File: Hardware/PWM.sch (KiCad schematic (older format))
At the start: 2 parts, among them U1 NLAS4599

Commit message: Renamed project
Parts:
- added D?: LED, symbol LED
- added R?: 250, symbol R
- added R?: 10K, symbol R
- added R?: 0, symbol R
- added TP?: TEST, symbol TEST
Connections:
- wire segments 13 -> 20
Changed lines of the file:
@@
 $Descr A4 11693 8268
 encoding utf-8
-Sheet 3 14
-Title ""
-Date ""
+Sheet 14 14
+Title "PWM Switching Circuit"
+Date "2017-05-13"
 Rev ""
-Comp ""
-Comment1 ""
+Comp "WARG"
+Comment1 "Author:Stephen Cholvat"
 Comment2 ""
 Comment3 ""
@@
 AR Path="/5919E173/5917D576" Ref="P?"  Part="1"
 AR Path="/591E6415/591EA448/5917D576" Ref="P?"  Part="1"
+AR Path="/591E6415/591EA45A/5917D576" Ref="P?"  Part="1"
+AR Path="/591E6415/591EA50E/5917D576" Ref="P?"  Part="1"
 F 0 "P?" H 6350 2600 50  0001 C CNN
 F 1 "PWM" V 6450 2400 50  0000 C CNN
@@
 AR Path="/5919E173/5917D57C" Ref="U1"  Part="1"
 AR Path="/591E6415/591EA448/5917D57C" Ref="U1"  Part="1"
+AR Path="/591E6415/591EA45A/5917D57C" Ref="U1"  Part="1"
+AR Path="/591E6415/591EA50E/5917D57C" Ref="U1"  Part="1"
 F 0 "U1" H 4500 3250 60  0000 C CNN
 F 1 "NLAS4599" H 4550 2500 60  0000 C CNN
@@
 $EndComp
 Wire Wire Line
-	4900 2500 5100 2500
-Wire Wire Line
-	5100 2500 6150 2500
+	4900 2500 6150 2500
 $Comp
 L GND #PWR?
@@
 AR Path="/5919E173/5917D836" Ref="#PWR?"  Part="1"
 AR Path="/591E6415/591EA448/5917D836" Ref="#PWR?"  Part="1"
+AR Path="/591E6415/591EA45A/5917D836" Ref="#PWR?"  Part="1"
+AR Path="/591E6415/591EA50E/5917D836" Ref="#PWR?"  Part="1"
 F 0 "#PWR?" H 5100 2450 50  0001 C CNN
 F 1 "GND" H 5100 2550 50  0000 C CNN
@@
 AR Path="/5919E173/5917D84C" Ref="#PWR?"  Part="1"
 AR Path="/591E6415/591EA448/5917D84C" Ref="#PWR?"  Part="1"
+AR Path="/591E6415/591EA45A/5917D84C" Ref="#PWR?"  Part="1"
+AR Path="/591E6415/591EA50E/5917D84C" Ref="#PWR?"  Part="1"
 F 0 "#PWR?" H 5100 1750 50  0001 C CNN
 F 1 "+5V" H 5100 2040 50  0000 C CNN
@@
 Text HLabel 5750 1950 1    60   Input ~ 0
 PWM_5V
-Text HLabel 3050 2450 0    60   Input ~ 0
+Text HLabel 2750 2450 0    60   Input ~ 0
 SEL
-Text HLabel 3050 2250 0    60   Input ~ 0
+Text HLabel 2750 2250 0    60   Input ~ 0
 PWM
-Text HLabel 3050 2150 0    60   Input ~ 0
+Text HLabel 2750 2150 0    60   Input ~ 0
 OC
 Wire Wire Line
-	3050 2150 4100 2150
-Wire Wire Line
-	3050 2250 4100 2250
-Wire Wire Line
-	3050 2450 4100 2450
+	2750 2150 4100 2150
+Wire Wire Line
+	2750 2250 4100 2250
+Wire Wire Line
+	2750 2450 3650 2450
 Wire Wire Line
 	4900 2200 4900 2300
 Wire Wire Line
 	4900 2300 6150 2300
+$Comp
+L LED D?
+U 1 1 591EF19A
+P 3550 3000
+AR Path="/591E6415/591EA448/591EF19A" Ref="D?"  Part="1"
+AR Path="/591E6415/591EA50E/591EF19A" Ref="D?"  Part="1"
+F 0 "D?" H 3550 3100 50  0000 C CNN
+F 1 "LED" H 3550 2900 50  0000 C CNN
+F 2 "" H 3550 3000 50  0000 C CNN
+F 3 "" H 3550 3000 50  0000 C CNN
+	1    3550 3000
+	0    -1   -1   0
+$EndComp
+$Comp
+L R R?
+U 1 1 591EF2D3
+P 3550 2650
+AR Path="/591E6415/591EA448/591EF2D3" Ref="R?"  Part="1"
+AR Path="/591E6415/591EA50E/591EF2D3" Ref="R?"  Part="1"
+F 0 "R?" V 3630 2650 50  0000 C CNN
+F 1 "250" V 3550 2650 50  0000 C CNN
+F 2 "" V 3480 2650 50  0000 C CNN
+F 3 "" H 3550 2650 50  0000 C CNN
+	1    3550 2650
+	1    0    0    -1
+$EndComp
+Wire Wire Line
+	3550 2800 3550 2850
+Wire Wire Line
+	3550 2450 3550 2500
+Connection ~ 3550 2450
+$Comp
+L GND #PWR?
+U 1 1 591EF3D9
+P 3350 3200
+AR Path="/591E6415/591EA448/591EF3D9" Ref="#PWR?"  Part="1"
+AR Path="/591E6415/591EA50E/591EF3D9" Ref="#PWR?"  Part="1"
+F 0 "#PWR?" H 3350 2950 50  0001 C CNN
+F 1 "GND" H 3350 3050 50  0000 C CNN
+F 2 "" H 3350 3200 50  0000 C CNN
+F 3 "" H 3350 3200 50  0000 C CNN
+	1    3350 3200
+	1    0    0    -1
+$EndComp
+Wire Wire Line
+	3550 3200 3550 3150
+$Comp
+L R R?
+U 1 1 591F0A89
+P 3150 2650
+F 0 "R?" V 3230 2650 50  0000 C CNN
+F 1 "10K" V 3150 2650 50  0000 C CNN
+F 2 "" V 3080 2650 50  0000 C CNN
+F 3 "" H 3150 2650 50  0000 C CNN
+	1    3150 2650
+	1    0    0    -1
+$EndComp
+Wire Wire Line
+	3150 3200 3550 3200
+Wire Wire Line
+	3150 2800 3150 3200
+Connection ~ 3350 3200
+Wire Wire Line
+	3150 2500 3150 2450
+Connection ~ 3150 2450
+$Comp
+L R R?
+U 1 1 591F0BAE
+P 3800 2450
+F 0 "R?" V 3880 2450 50  0000 C CNN
+F 1 "0" V 3800 2450 50  0000 C CNN
+F 2 "" V 3730 2450 50  0000 C CNN
+F 3 "" H 3800 2450 50  0000 C CNN
+	1    3800 2450
+	0    1    1    0
+$EndComp
+Wire Wire Line
+	3950 2450 4100 2450
+Connection ~ 4000 2450
+$Comp
+L TEST TP?
+U 1 1 591F0CEF
+P 4000 2600
+F 0 "TP?" H 4000 2900 50  0000 C BNN
+F 1 "TEST" H 4000 2850 50  0000 C CNN
+F 2 "" H 4000 2600 50  0000 C CNN
+F 3 "" H 4000 2600 50  0000 C CNN
+	1    4000 2600
+	-1   0    0    1
+$EndComp
+Wire Wire Line
+	4000 2600 4000 2450
 $EndSCHEMATC

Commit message: ALL THE POWER
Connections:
- net labels added: SW_5V
- net labels removed: +5V
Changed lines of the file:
@@
 LIBS:valves
 LIBS:WARG
+LIBS:ZeroPilot-cache
 EELAYER 25 0
 EELAYER END
 $Descr A4 11693 8268
 encoding utf-8
-Sheet 14 14
+Sheet 14 15
 Title "PWM Switching Circuit"
 Date "2017-05-13"
@@
 AR Path="/591E6415/591EA45A/5917D576" Ref="P?"  Part="1"
 AR Path="/591E6415/591EA50E/5917D576" Ref="P?"  Part="1"
+AR Path="/591E6415/591EA490/5917D576" Ref="P?"  Part="1"
+AR Path="/591E6415/591EA46C/5917D576" Ref="P?"  Part="1"
+AR Path="/591E6415/591EA47E/5917D576" Ref="P?"  Part="1"
+AR Path="/591E6415/591EA4A2/5917D576" Ref="P?"  Part="1"
+AR Path="/591E6415/591EA4B4/5917D576" Ref="P?"  Part="1"
+AR Path="/591E6415/591EA4C6/5917D576" Ref="P?"  Part="1"
+AR Path="/591E6415/591EA4D8/5917D576" Ref="P?"  Part="1"
+AR Path="/591E6415/591EA4EA/5917D576" Ref="P?"  Part="1"
+AR Path="/591E6415/591EA4FC/5917D576" Ref="P?"  Part="1"
 F 0 "P?" H 6350 2600 50  0001 C CNN
 F 1 "PWM" V 6450 2400 50  0000 C CNN
@@
 AR Path="/591E6415/591EA45A/5917D57C" Ref="U1"  Part="1"
 AR Path="/591E6415/591EA50E/5917D57C" Ref="U1"  Part="1"
+AR Path="/591E6415/591EA490/5917D57C" Ref="U1"  Part="1"
+AR Path="/591E6415/591EA46C/5917D57C" Ref="U1"  Part="1"
+AR Path="/591E6415/591EA47E/5917D57C" Ref="U1"  Part="1"
+AR Path="/591E6415/591EA4A2/5917D57C" Ref="U1"  Part="1"
+AR Path="/591E6415/591EA4B4/5917D57C" Ref="U1"  Part="1"
+AR Path="/591E6415/591EA4C6/5917D57C" Ref="U1"  Part="1"
+AR Path="/591E6415/591EA4D8/5917D57C" Ref="U1"  Part="1"
+AR Path="/591E6415/591EA4EA/5917D57C" Ref="U1"  Part="1"
+AR Path="/591E6415/591EA4FC/5917D57C" Ref="U1"  Part="1"
 F 0 "U1" H 4500 3250 60  0000 C CNN
 F 1 "NLAS4599" H 4550 2500 60  0000 C CNN
@@
 AR Path="/591836F4/5917D836" Ref="#PWR?"  Part="1"
 AR Path="/5919E173/5917D836" Ref="#PWR?"  Part="1"
-AR Path="/591E6415/591EA448/5917D836" Ref="#PWR?"  Part="1"
-AR Path="/591E6415/591EA45A/5917D836" Ref="#PWR?"  Part="1"
-AR Path="/591E6415/591EA50E/5917D836" Ref="#PWR?"  Part="1"
-F 0 "#PWR?" H 5100 2450 50  0001 C CNN
+AR Path="/591E6415/591EA448/5917D836" Ref="#PWR01"  Part="1"
+AR Path="/591E6415/591EA45A/5917D836" Ref="#PWR03"  Part="1"
+AR Path="/591E6415/591EA50E/5917D836" Ref="#PWR023"  Part="1"
+AR Path="/591E6415/591EA490/5917D836" Ref="#PWR09"  Part="1"
+AR Path="/591E6415/591EA46C/5917D836" Ref="#PWR05"  Part="1"
+AR Path="/591E6415/591EA47E/5917D836" Ref="#PWR07"  Part="1"
+AR Path="/591E6415/591EA4A2/5917D836" Ref="#PWR011"  Part="1"
+AR Path="/591E6415/591EA4B4/5917D836" Ref="#PWR013"  Part="1"
+AR Path="/591E6415/591EA4C6/5917D836" Ref="#PWR015"  Part="1"
+AR Path="/591E6415/591EA4D8/5917D836" Ref="#PWR017"  Part="1"
+AR Path="/591E6415/591EA4EA/5917D836" Ref="#PWR019"  Part="1"
+AR Path="/591E6415/591EA4FC/5917D836" Ref="#PWR021"  Part="1"
+F 0 "#PWR023" H 5100 2450 50  0001 C CNN
 F 1 "GND" H 5100 2550 50  0000 C CNN
 F 2 "" H 5100 2700 50  0000 C CNN
@@
 	1    0    0    -1
 $EndComp
-$Comp
-L +5V #PWR?
-U 1 1 5917D84C
-P 5100 1900
-AR Path="/5917CEAC/5917D84C" Ref="#PWR?"  Part="1"
-AR Path="/5917EAD8/5917D84C" Ref="#PWR?"  Part="1"
-AR Path="/5917F7DD/5917D84C" Ref="#PWR?"  Part="1"
-AR Path="/591836F4/5917D84C" Ref="#PWR?"  Part="1"
-AR Path="/5919E173/5917D84C" Ref="#PWR?"  Part="1"
-AR Path="/591E6415/591EA448/5917D84C" Ref="#PWR?"  Part="1"
-AR Path="/591E6415/591EA45A/5917D84C" Ref="#PWR?"  Part="1"
-AR Path="/591E6415/591EA50E/5917D84C" Ref="#PWR?"  Part="1"
-F 0 "#PWR?" H 5100 1750 50  0001 C CNN
-F 1 "+5V" H 5100 2040 50  0000 C CNN
-F 2 "" H 5100 1900 50  0000 C CNN
-F 3 "" H 5100 1900 50  0000 C CNN
-	1    5100 1900
-	1    0    0    -1
-$EndComp
 Wire Wire Line
 	4900 2200 4900 2200
@@
 Wire Wire Line
 	4900 2400 5100 2400
-Wire Wire Line
-	5100 2400 5100 1900
 Wire Wire Line
 	5100 2700 5100 2500
@@
 AR Path="/591E6415/591EA448/591EF19A" Ref="D?"  Part="1"
 AR Path="/591E6415/591EA50E/591EF19A" Ref="D?"  Part="1"
+AR Path="/591E6415/591EA490/591EF19A" Ref="D?"  Part="1"
+AR Path="/591E6415/591EA45A/591EF19A" Ref="D?"  Part="1"
+AR Path="/591E6415/591EA46C/591EF19A" Ref="D?"  Part="1"
+AR Path="/591E6415/591EA47E/591EF19A" Ref="D?"  Part="1"
+AR Path="/591E6415/591EA4A2/591EF19A" Ref="D?"  Part="1"
+AR Path="/591E6415/591EA4B4/591EF19A" Ref="D?"  Part="1"
+AR Path="/591E6415/591EA4C6/591EF19A" Ref="D?"  Part="1"
+AR Path="/591E6415/591EA4D8/591EF19A" Ref="D?"  Part="1"
+AR Path="/591E6415/591EA4EA/591EF19A" Ref="D?"  Part="1"
+AR Path="/591E6415/591EA4FC/591EF19A" Ref="D?"  Part="1"
 F 0 "D?" H 3550 3100 50  0000 C CNN
 F 1 "LED" H 3550 2900 50  0000 C CNN
@@
 AR Path="/591E6415/591EA448/591EF2D3" Ref="R?"  Part="1"
 AR Path="/591E6415/591EA50E/591EF2D3" Ref="R?"  Part="1"
+AR Path="/591E6415/591EA490/591EF2D3" Ref="R?"  Part="1"
+AR Path="/591E6415/591EA45A/591EF2D3" Ref="R?"  Part="1"
+AR Path="/591E6415/591EA46C/591EF2D3" Ref="R?"  Part="1"
+AR Path="/591E6415/591EA47E/591EF2D3" Ref="R?"  Part="1"
+AR Path="/591E6415/591EA4A2/591EF2D3" Ref="R?"  Part="1"
+AR Path="/591E6415/591EA4B4/591EF2D3" Ref="R?"  Part="1"
+AR Path="/591E6415/591EA4C6/591EF2D3" Ref="R?"  Part="1"
+AR Path="/591E6415/591EA4D8/591EF2D3" Ref="R?"  Part="1"
+AR Path="/591E6415/591EA4EA/591EF2D3" Ref="R?"  Part="1"
+AR Path="/591E6415/591EA4FC/591EF2D3" Ref="R?"  Part="1"
 F 0 "R?" V 3630 2650 50  0000 C CNN
 F 1 "250" V 3550 2650 50  0000 C CNN
@@
 Connection ~ 3550 2450
 $Comp
-L GND #PWR?
+L GND #PWR02
 U 1 1 591EF3D9
 P 3350 3200
-AR Path="/591E6415/591EA448/591EF3D9" Ref="#PWR?"  Part="1"
-AR Path="/591E6415/591EA50E/591EF3D9" Ref="#PWR?"  Part="1"
-F 0 "#PWR?" H 3350 2950 50  0001 C CNN
+AR Path="/591E6415/591EA448/591EF3D9" Ref="#PWR02"  Part="1"
+AR Path="/591E6415/591EA50E/591EF3D9" Ref="#PWR024"  Part="1"
+AR Path="/591E6415/591EA490/591EF3D9" Ref="#PWR010"  Part="1"
+AR Path="/591E6415/591EA45A/591EF3D9" Ref="#PWR04"  Part="1"
+AR Path="/591E6415/591EA46C/591EF3D9" Ref="#PWR06"  Part="1"
+AR Path="/591E6415/591EA47E/591EF3D9" Ref="#PWR08"  Part="1"
+AR Path="/591E6415/591EA4A2/591EF3D9" Ref="#PWR012"  Part="1"
+AR Path="/591E6415/591EA4B4/591EF3D9" Ref="#PWR014"  Part="1"
+AR Path="/591E6415/591EA4C6/591EF3D9" Ref="#PWR016"  Part="1"
+AR Path="/591E6415/591EA4D8/591EF3D9" Ref="#PWR018"  Part="1"
+AR Path="/591E6415/591EA4EA/591EF3D9" Ref="#PWR020"  Part="1"
+AR Path="/591E6415/591EA4FC/591EF3D9" Ref="#PWR022"  Part="1"
+F 0 "#PWR024" H 3350 2950 50  0001 C CNN
 F 1 "GND" H 3350 3050 50  0000 C CNN
 F 2 "" H 3350 3200 50  0000 C CNN
@@
 U 1 1 591F0A89
 P 3150 2650
+AR Path="/591E6415/591EA50E/591F0A89" Ref="R?"  Part="1"
+AR Path="/591E6415/591EA448/591F0A89" Ref="R?"  Part="1"
+AR Path="/591E6415/591EA45A/591F0A89" Ref="R?"  Part="1"
+AR Path="/591E6415/591EA46C/591F0A89" Ref="R?"  Part="1"
+AR Path="/591E6415/591EA47E/591F0A89" Ref="R?"  Part="1"
+AR Path="/591E6415/591EA490/591F0A89" Ref="R?"  Part="1"
+AR Path="/591E6415/591EA4A2/591F0A89" Ref="R?"  Part="1"
+AR Path="/591E6415/591EA4B4/591F0A89" Ref="R?"  Part="1"
+AR Path="/591E6415/591EA4C6/591F0A89" Ref="R?"  Part="1"
+AR Path="/591E6415/591EA4D8/591F0A89" Ref="R?"  Part="1"
+AR Path="/591E6415/591EA4EA/591F0A89" Ref="R?"  Part="1"
+AR Path="/591E6415/591EA4FC/591F0A89" Ref="R?"  Part="1"
 F 0 "R?" V 3230 2650 50  0000 C CNN
 F 1 "10K" V 3150 2650 50  0000 C CNN
@@
 U 1 1 591F0BAE
 P 3800 2450
+AR Path="/591E6415/591EA50E/591F0BAE" Ref="R?"  Part="1"
+AR Path="/591E6415/591EA448/591F0BAE" Ref="R?"  Part="1"
+AR Path="/591E6415/591EA45A/591F0BAE" Ref="R?"  Part="1"
+AR Path="/591E6415/591EA46C/591F0BAE" Ref="R?"  Part="1"
+AR Path="/591E6415/591EA47E/591F0BAE" Ref="R?"  Part="1"
+AR Path="/591E6415/591EA490/591F0BAE" Ref="R?"  Part="1"
+AR Path="/591E6415/591EA4A2/591F0BAE" Ref="R?"  Part="1"
+AR Path="/591E6415/591EA4B4/591F0BAE" Ref="R?"  Part="1"
+AR Path="/591E6415/591EA4C6/591F0BAE" Ref="R?"  Part="1"
+AR Path="/591E6415/591EA4D8/591F0BAE" Ref="R?"  Part="1"
+AR Path="/591E6415/591EA4EA/591F0BAE" Ref="R?"  Part="1"
+AR Path="/591E6415/591EA4FC/591F0BAE" Ref="R?"  Part="1"
 F 0 "R?" V 3880 2450 50  0000 C CNN
 F 1 "0" V 3800 2450 50  0000 C CNN
@@
 U 1 1 591F0CEF
 P 4000 2600
+AR Path="/591E6415/591EA50E/591F0CEF" Ref="TP?"  Part="1"
+AR Path="/591E6415/591EA448/591F0CEF" Ref="TP?"  Part="1"
+AR Path="/591E6415/591EA45A/591F0CEF" Ref="TP?"  Part="1"
+AR Path="/591E6415/591EA46C/591F0CEF" Ref="TP?"  Part="1"
+AR Path="/591E6415/591EA47E/591F0CEF" Ref="TP?"  Part="1"
+AR Path="/591E6415/591EA490/591F0CEF" Ref="TP?"  Part="1"
+AR Path="/591E6415/591EA4A2/591F0CEF" Ref="TP?"  Part="1"
+AR Path="/591E6415/591EA4B4/591F0CEF" Ref="TP?"  Part="1"
+AR Path="/591E6415/591EA4C6/591F0CEF" Ref="TP?"  Part="1"
+AR Path="/591E6415/591EA4D8/591F0CEF" Ref="TP?"  Part="1"
+AR Path="/591E6415/591EA4EA/591F0CEF" Ref="TP?"  Part="1"
+AR Path="/591E6415/591EA4FC/591F0CEF" Ref="TP?"  Part="1"
 F 0 "TP?" H 4000 2900 50  0000 C BNN
 F 1 "TEST" H 4000 2850 50  0000 C CNN
@@
 Wire Wire Line
 	4000 2600 4000 2450
+Text HLabel 5100 1950 1    60   Input ~ 0
+SW_5V
+Wire Wire Line
+	5100 2400 5100 1950
 $EndSCHEMATC

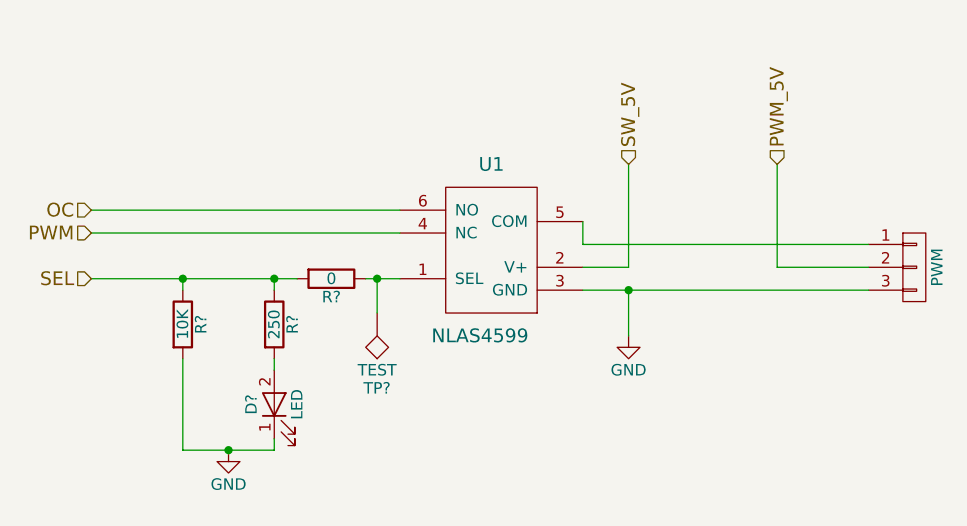
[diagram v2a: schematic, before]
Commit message: Added F7 chip
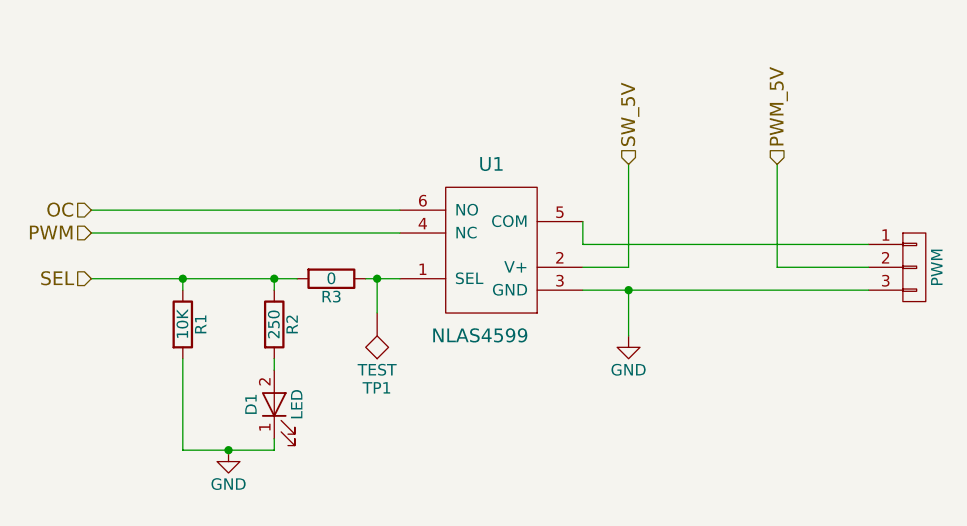
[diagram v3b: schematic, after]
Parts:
- gave numbers to parts that had none: 6
